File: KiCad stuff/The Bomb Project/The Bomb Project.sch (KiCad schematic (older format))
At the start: 17 parts

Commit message: Add and use HT16K33
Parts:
- removed Q? (x8): Q_NMOS_GSD, symbol Device:Q_NMOS_GSD
- removed U? (x4): 74LS573, symbol 74xx:74LS573
- removed U?: HDSP-B09G, The Gelsoft Bomb Project:HDSP-B08G, symbol The~Gelsoft~Bomb~Project:HDSP-B09G
- added U?: HT16K33_SOP28, The Gelsoft Bomb Project:SOP-28_7.5x15.4mm_P1.27mm, symbol The~Gelsoft~Bomb~Project:HT16K33_SOP28
- added U?: HDSP-B08G, The Gelsoft Bomb Project:HDSP-B08G, symbol The~Gelsoft~Bomb~Project:HDSP-B08G
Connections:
- wire segments 144 -> 25

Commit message: Add and use MAX7219
Chips ahoy!

Finally found the one we should be using. The 7219 supports up to 8 digits *including* decimal places *and* it uses a shift register with latches and current sourcing/sinking built in! It's the perfect chip and available from China at ~$1 AUD a pop.
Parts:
- removed U?: HT16K33_SOP28, The Gelsoft Bomb Project:SOP-28_7.5x15.4mm_P1.27mm, symbol The~Gelsoft~Bomb~Project:HT16K33_SOP28
- added R?: 20k, symbol Device:R
- added U?: MAX7219, symbol The~Gelsoft~Bomb~Project:MAX7219
- U?: value HDSP-B08G -> HDSP-B09G; symbol The~Gelsoft~Bomb~Project:HDSP-B08G -> The~Gelsoft~Bomb~Project:HDSP-B09G
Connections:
- net labels removed: D1EN, D2EN, D3EN, D4EN
- wire segments 25 -> 46
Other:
- moved on the sheet: BZ?, J?, U?

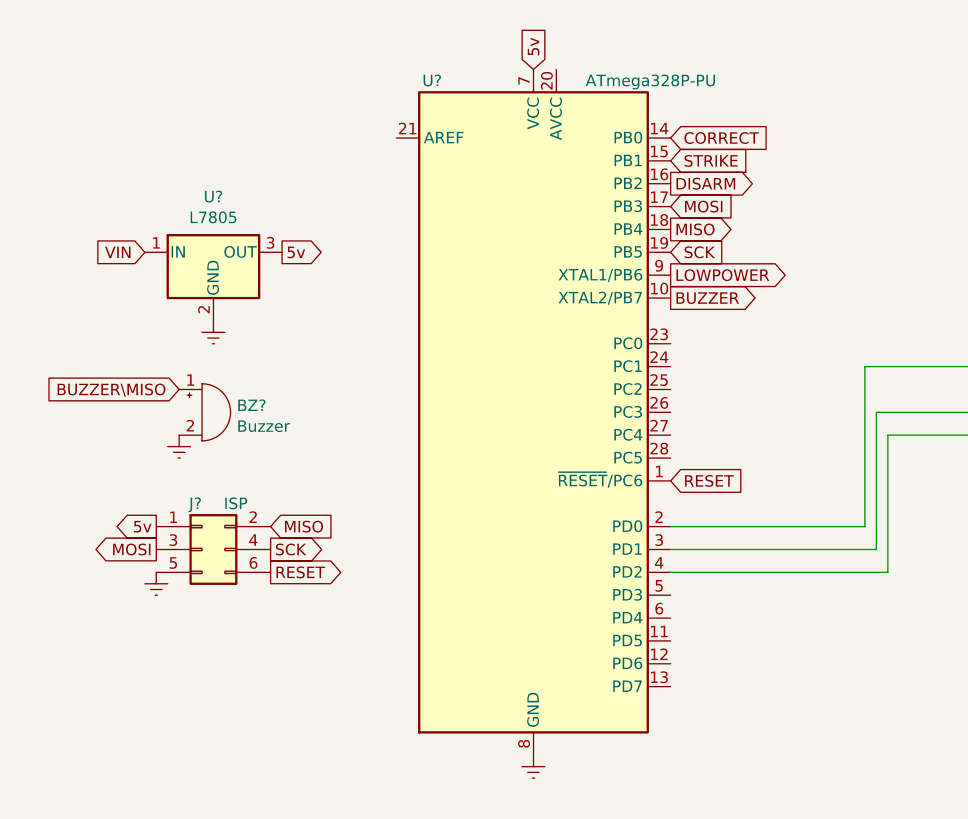
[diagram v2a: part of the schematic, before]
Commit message: Downgrade MCU to an ATTiny24A
We don't need all of the extra features on a Mega328P, the Tiny24A should do it just fine
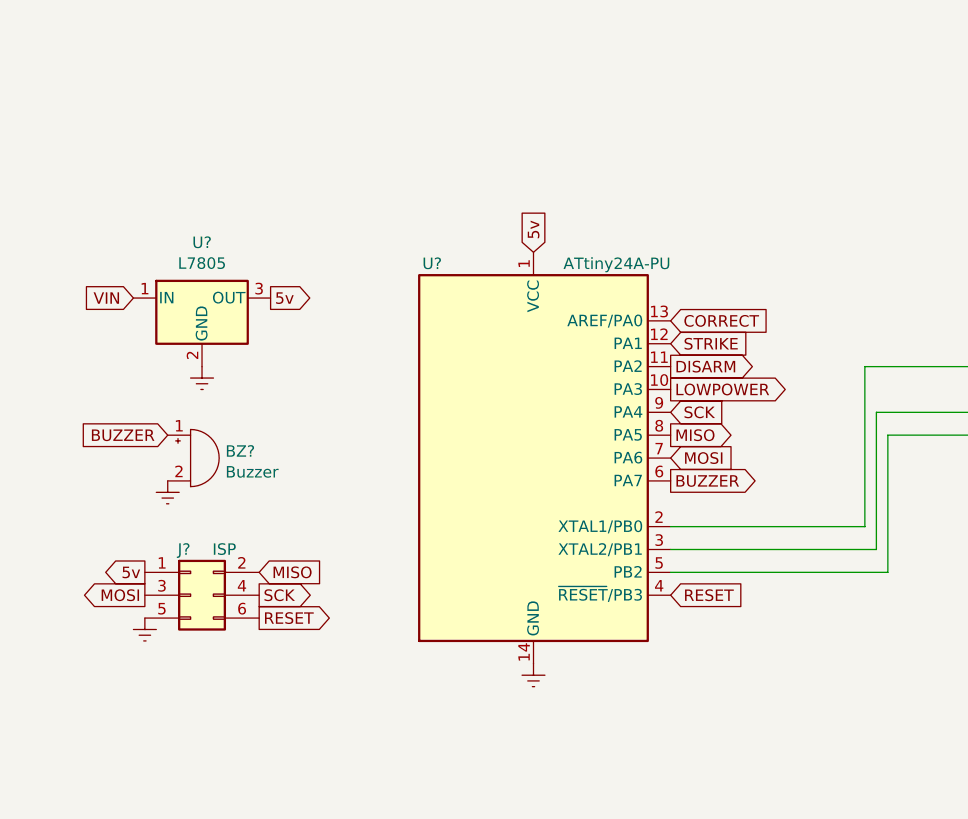
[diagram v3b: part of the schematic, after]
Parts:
- removed U?: ATmega328P-PU, Package_DIP:DIP-28_W7.62mm, symbol MCU_Microchip_ATmega:ATmega328P-PU
- added U?: ATtiny24A-PU, Package_DIP:DIP-14_W7.62mm, symbol MCU_Microchip_ATtiny:ATtiny24A-PU
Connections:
- net labels removed: BUZZER\MISO
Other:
- moved on the sheet: BZ?, J?, U?
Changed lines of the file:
@@
 L Connector_Generic:Conn_02x03_Odd_Even J?
 U 1 1 5D7346A6
-P 1650 4400
-F 0 "J?" H 1650 4600 50  0000 R CNN
-F 1 "ISP" H 1850 4600 50  0000 R CNN
-F 2 "" H 1650 4400 50  0001 C CNN
-F 3 "~" H 1650 4400 50  0001 C CNN
-	1    1650 4400
-	1    0    0    -1
-$EndComp
-Text GLabel 1450 4300 0    50   Output ~ 0
-5v
-Text GLabel 1450 4400 0    50   Output ~ 0
+P 1600 4600
+F 0 "J?" H 1600 4800 50  0000 R CNN
+F 1 "ISP" H 1800 4800 50  0000 R CNN
+F 2 "" H 1600 4600 50  0001 C CNN
+F 3 "~" H 1600 4600 50  0001 C CNN
+	1    1600 4600
+	1    0    0    -1
+$EndComp
+Text GLabel 1400 4500 0    50   Output ~ 0
+5v
+Text GLabel 1400 4600 0    50   Output ~ 0
 MOSI
-Text GLabel 1950 4300 2    50   Input ~ 0
+Text GLabel 1900 4500 2    50   Input ~ 0
 MISO
-Text GLabel 1950 4400 2    50   Output ~ 0
+Text GLabel 1900 4600 2    50   Output ~ 0
 SCK
-Text GLabel 1950 4500 2    50   Output ~ 0
+Text GLabel 1900 4700 2    50   Output ~ 0
 RESET
-Text GLabel 3100 2300 1    50   Input ~ 0
+Text GLabel 3100 3100 1    50   Input ~ 0
 5v
 $Comp
 L power:Earth #PWR?
 U 1 1 5D74824F
-P 1450 4500
-F 0 "#PWR?" H 1450 4250 50  0001 C CNN
-F 1 "Earth" H 1450 4350 50  0001 C CNN
-F 2 "" H 1450 4500 50  0001 C CNN
-F 3 "~" H 1450 4500 50  0001 C CNN
-	1    1450 4500
+P 1400 4700
+F 0 "#PWR?" H 1400 4450 50  0001 C CNN
+F 1 "Earth" H 1400 4550 50  0001 C CNN
+F 2 "" H 1400 4700 50  0001 C CNN
+F 3 "~" H 1400 4700 50  0001 C CNN
+	1    1400 4700
 	1    0    0    -1
 $EndComp
@@
 L power:Earth #PWR?
 U 1 1 5D748395
-P 3100 5300
-F 0 "#PWR?" H 3100 5050 50  0001 C CNN
-F 1 "Earth" H 3100 5150 50  0001 C CNN
-F 2 "" H 3100 5300 50  0001 C CNN
-F 3 "~" H 3100 5300 50  0001 C CNN
-	1    3100 5300
+P 3100 4900
+F 0 "#PWR?" H 3100 4650 50  0001 C CNN
+F 1 "Earth" H 3100 4750 50  0001 C CNN
+F 2 "" H 3100 4900 50  0001 C CNN
+F 3 "~" H 3100 4900 50  0001 C CNN
+	1    3100 4900
 	1    0    0    -1
 $EndComp
@@
 L Regulator_Linear:L7805 U?
 U 1 1 5D74AD90
-P 1700 3100
-F 0 "U?" H 1700 3342 50  0000 C CNN
-F 1 "L7805" H 1700 3251 50  0000 C CNN
-F 2 "" H 1725 2950 50  0001 L CIN
-F 3 "http://www.st.com/content/ccc/resource/technical/document/datasheet/41/4f/b3/b0/12/d4/47/88/CD00000444.pdf/files/CD00000444.pdf/jcr:content/translations/en.CD00000444.pdf" H 1700 3050 50  0001 C CNN
-	1    1700 3100
-	1    0    0    -1
-$EndComp
-Text GLabel 1400 3100 0    50   Input ~ 0
+P 1650 3300
+F 0 "U?" H 1650 3542 50  0000 C CNN
+F 1 "L7805" H 1650 3451 50  0000 C CNN
+F 2 "" H 1675 3150 50  0001 L CIN
+F 3 "http://www.st.com/content/ccc/resource/technical/document/datasheet/41/4f/b3/b0/12/d4/47/88/CD00000444.pdf/files/CD00000444.pdf/jcr:content/translations/en.CD00000444.pdf" H 1650 3250 50  0001 C CNN
+	1    1650 3300
+	1    0    0    -1
+$EndComp
+Text GLabel 1350 3300 0    50   Input ~ 0
 VIN
-Text GLabel 2000 3100 2    50   Output ~ 0
+Text GLabel 1950 3300 2    50   Output ~ 0
 5v
 $Comp
 L power:Earth #PWR?
 U 1 1 5D74BAAF
-P 1700 3400
-F 0 "#PWR?" H 1700 3150 50  0001 C CNN
-F 1 "Earth" H 1700 3250 50  0001 C CNN
-F 2 "" H 1700 3400 50  0001 C CNN
-F 3 "~" H 1700 3400 50  0001 C CNN
-	1    1700 3400
-	1    0    0    -1
-$EndComp
-Text GLabel 3700 3000 2    50   Output ~ 0
+P 1650 3600
+F 0 "#PWR?" H 1650 3350 50  0001 C CNN
+F 1 "Earth" H 1650 3450 50  0001 C CNN
+F 2 "" H 1650 3600 50  0001 C CNN
+F 3 "~" H 1650 3600 50  0001 C CNN
+	1    1650 3600
+	1    0    0    -1
+$EndComp
+Text GLabel 3700 3900 2    50   Output ~ 0
 MISO
-Text GLabel 3700 4100 2    50   Input ~ 0
+Text GLabel 3700 4600 2    50   Input ~ 0
 RESET
-Text GLabel 3700 3100 2    50   Input ~ 0
+Text GLabel 3700 3800 2    50   Input ~ 0
 SCK
-Text GLabel 3700 2700 2    50   Input ~ 0
+Text GLabel 3700 3500 2    50   Input ~ 0
 STRIKE
-Text GLabel 3700 2800 2    50   Output ~ 0
+Text GLabel 3700 3600 2    50   Output ~ 0
 DISARM
-Text GLabel 3700 2900 2    50   Input ~ 0
+Text GLabel 3700 4000 2    50   Input ~ 0
 MOSI
 $Comp
 L Device:Buzzer BZ?
 U 1 1 5D77FD04
-P 1650 3800
-F 0 "BZ?" H 1802 3829 50  0000 L CNN
-F 1 "Buzzer" H 1802 3738 50  0000 L CNN
-F 2 "" V 1625 3900 50  0001 C CNN
-F 3 "~" V 1625 3900 50  0001 C CNN
-	1    1650 3800
+P 1600 4000
+F 0 "BZ?" H 1752 4029 50  0000 L CNN
+F 1 "Buzzer" H 1752 3938 50  0000 L CNN
+F 2 "" V 1575 4100 50  0001 C CNN
+F 3 "~" V 1575 4100 50  0001 C CNN
+	1    1600 4000
 	1    0    0    -1
 $EndComp
@@
 L power:Earth #PWR?
 U 1 1 5D780156
-P 1550 3900
-F 0 "#PWR?" H 1550 3650 50  0001 C CNN
-F 1 "Earth" H 1550 3750 50  0001 C CNN
-F 2 "" H 1550 3900 50  0001 C CNN
-F 3 "~" H 1550 3900 50  0001 C CNN
-	1    1550 3900
-	1    0    0    -1
-$EndComp
-Text GLabel 1550 3700 0    50   Input ~ 0
-BUZZER\MISO
-$Comp
-L MCU_Microchip_ATmega:ATmega328P-PU U?
-U 1 1 5D738683
-P 3100 3800
-F 0 "U?" H 2700 5250 50  0000 R CNN
-F 1 "ATmega328P-PU" H 3900 5250 50  0000 R CNN
-F 2 "Package_DIP:DIP-28_W7.62mm" H 3100 3800 50  0001 C CIN
-F 3 "http://ww1.microchip.com/downloads/en/DeviceDoc/ATmega328_P%20AVR%20MCU%20with%20picoPower%20Technology%20Data%20Sheet%2040001984A.pdf" H 3100 3800 50  0001 C CNN
-	1    3100 3800
-	1    0    0    -1
-$EndComp
-Text GLabel 3700 3300 2    50   Output ~ 0
+P 1500 4100
+F 0 "#PWR?" H 1500 3850 50  0001 C CNN
+F 1 "Earth" H 1500 3950 50  0001 C CNN
+F 2 "" H 1500 4100 50  0001 C CNN
+F 3 "~" H 1500 4100 50  0001 C CNN
+	1    1500 4100
+	1    0    0    -1
+$EndComp
+Text GLabel 1500 3900 0    50   Input ~ 0
 BUZZER
-Text GLabel 3700 3200 2    50   Output ~ 0
+Text GLabel 3700 4100 2    50   Output ~ 0
+BUZZER
+Text GLabel 3700 3700 2    50   Output ~ 0
 LOWPOWER
-Text GLabel 3700 2600 2    50   Input ~ 0
+Text GLabel 3700 3400 2    50   Input ~ 0
 CORRECT
 $Comp
@@
 Wire Wire Line
 	4650 4500 3700 4500
+$Comp
+L MCU_Microchip_ATtiny:ATtiny24A-PU U?
+U 1 1 5D807087
+P 3100 4000
+F 0 "U?" H 2700 4850 50  0000 R CNN
+F 1 "ATtiny24A-PU" H 3700 4850 50  0000 R CNN
+F 2 "Package_DIP:DIP-14_W7.62mm" H 3100 4000 50  0001 C CIN
+F 3 "http://ww1.microchip.com/downloads/en/DeviceDoc/doc8183.pdf" H 3100 4000 50  0001 C CNN
+	1    3100 4000
+	1    0    0    -1
+$EndComp
 $EndSCHEMATC

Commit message: Add RS232 connector and finalise schematic
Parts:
- added J?: DB9 Male, symbol Connector:DB9_Male
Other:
- moved on the sheet: BZ?, J?, R?, U?

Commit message: Add battery connector
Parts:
- added J?: Battery Header, symbol Connector:Conn_01x02_Male
- J?: value DB9 Male -> Module Connector
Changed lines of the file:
@@
 U 1 1 5D74AD90
 P 1900 2700
-F 0 "U?" H 1900 2942 50  0000 C CNN
-F 1 "L7805" H 1900 2851 50  0000 C CNN
+F 0 "U?" H 1750 2850 50  0000 C CNN
+F 1 "L7805" H 2050 2850 50  0000 C CNN
 F 2 "" H 1925 2550 50  0001 L CIN
 F 3 "http://www.st.com/content/ccc/resource/technical/document/datasheet/41/4f/b3/b0/12/d4/47/88/CD00000444.pdf/files/CD00000444.pdf/jcr:content/translations/en.CD00000444.pdf" H 1900 2650 50  0001 C CNN
@@
 P 2000 5150
 F 0 "J?" H 1800 5750 50  0000 L CNN
-F 1 "DB9 Male" H 2000 5750 50  0000 L CNN
+F 1 "Module Connector" H 2000 5750 50  0000 L CNN
 F 2 "" H 2000 5150 50  0001 C CNN
 F 3 " ~" H 2000 5150 50  0001 C CNN
@@
 	1    0    0    -1
 $EndComp
+$Comp
+L Connector:Conn_01x02_Male J?
+U 1 1 5D74C8FE
+P 2000 6150
+F 0 "J?" H 1972 6032 50  0000 R CNN
+F 1 "Battery Header" H 1972 6123 50  0000 R CNN
+F 2 "" H 2000 6150 50  0001 C CNN
+F 3 "~" H 2000 6150 50  0001 C CNN
+	1    2000 6150
+	-1   0    0    1
+$EndComp
+Text GLabel 1800 6050 0    50   Output ~ 0
+VIN
+$Comp
+L power:Earth #PWR?
+U 1 1 5D750EEE
+P 1800 6150
+F 0 "#PWR?" H 1800 5900 50  0001 C CNN
+F 1 "Earth" H 1800 6000 50  0001 C CNN
+F 2 "" H 1800 6150 50  0001 C CNN
+F 3 "~" H 1800 6150 50  0001 C CNN
+	1    1800 6150
+	1    0    0    -1
+$EndComp
